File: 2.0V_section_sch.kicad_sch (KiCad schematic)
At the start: 1 part, among them U3_5 TPS259620DDAR

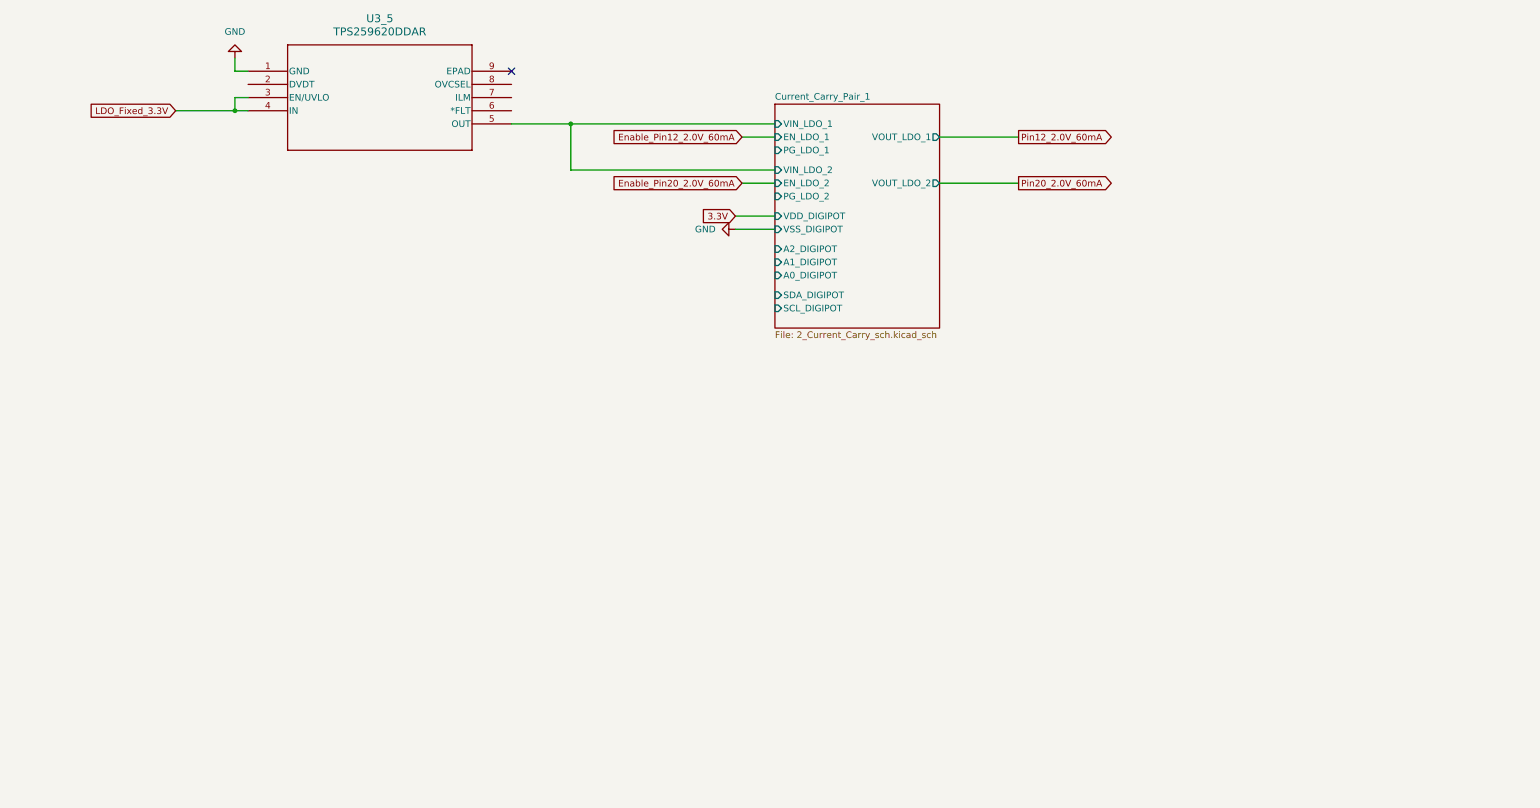
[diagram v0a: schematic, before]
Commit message: Full schematic connection without ratio consideration.
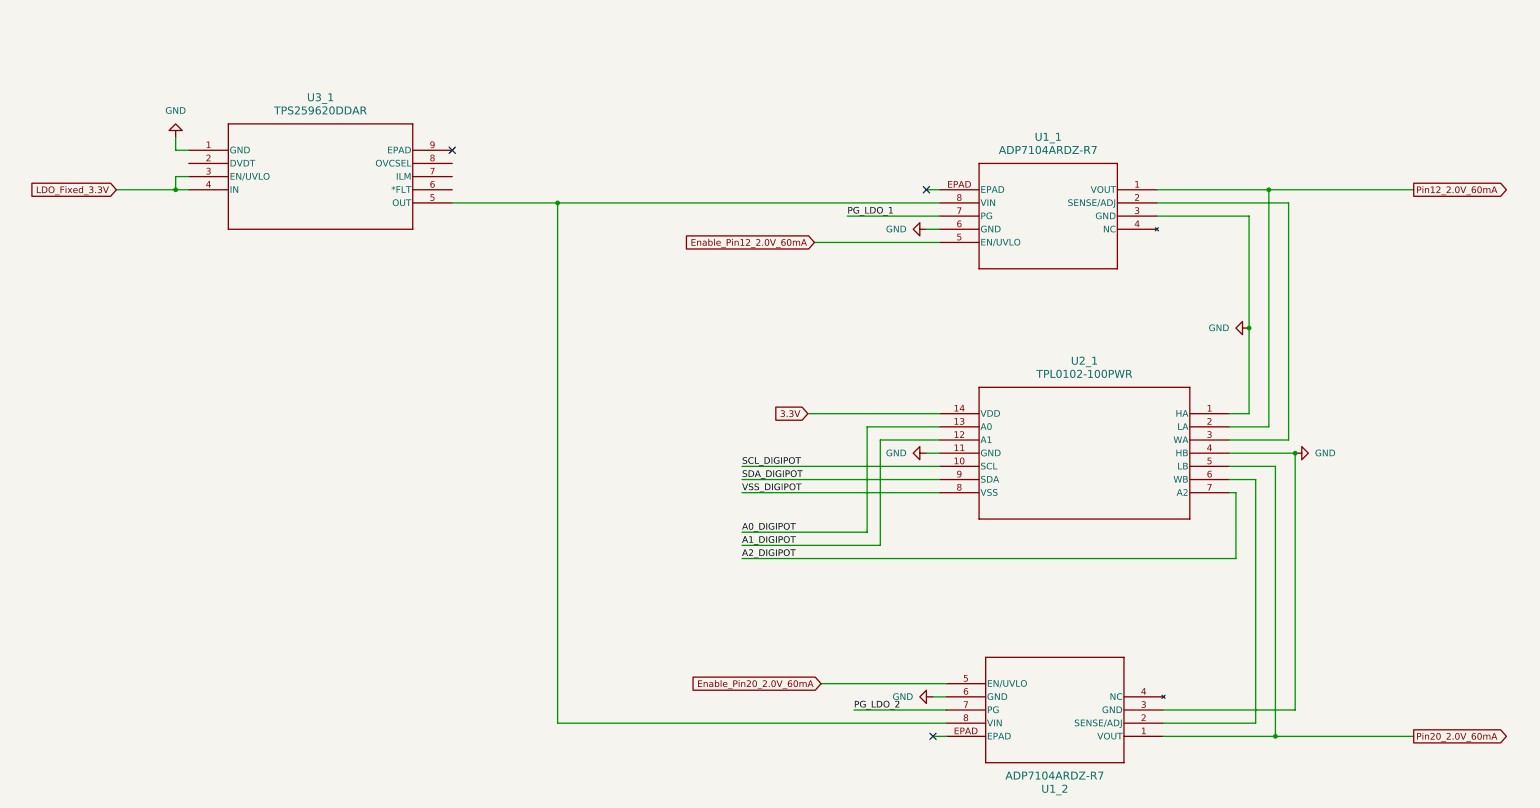
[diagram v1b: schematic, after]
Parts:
- removed U3_5: TPS259620DDAR, SOIC_20DDAR_TEX, symbol eFuse for electronic:TPS259620DDAR
- added U1_1, U1_2: ADP7104ARDZ-R7, RD_8_2_ADI, symbol Adjustable Low-Dropout Regulator:ADP7104ARDZ-R7
- added U2_1: TPL0102-100PWR, PW14, symbol Digital Potentiometer:TPL0102-100PWR
- added U3_1: TPS259620DDAR, SOIC_20DDAR_TEX, symbol eFuse for electronic:TPS259620DDAR
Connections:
- net 3.3V: now also U2_1.14 (VDD)
- net Enable_Pin12_2.0V_60mA: now also U1_1.5 (EN/UVLO)
- net Enable_Pin20_2.0V_60mA: now also U1_2.5 (EN/UVLO)
- net GND: now also U1_1.3 (GND), U1_1.6 (GND), U1_2.3 (GND), U1_2.6 (GND), U2_1.1 (HA), U2_1.11 (GND), U2_1.4 (HB), U3_1.1 (GND)
- net LDO_Fixed_3.3V: now also U3_1.3 (EN/UVLO), U3_1.4 (IN)
- net Pin12_2.0V_60mA: now also U1_1.1 (VOUT), U2_1.2 (LA)
- net Pin20_2.0V_60mA: now also U1_2.1 (VOUT), U2_1.5 (LB)
- new net: U1_1.2 (SENSE/ADJ), U2_1.3 (WA)
- new net: U1_1.8 (VIN), U1_2.8 (VIN), U3_1.5 (OUT)
- new net: U1_2.2 (SENSE/ADJ), U2_1.6 (WB)
- new net A0_DIGIPOT: U2_1.13 (A0)
- new net A1_DIGIPOT: U2_1.12 (A1)
- new net A2_DIGIPOT: U2_1.7 (A2)
- new net PG_LDO_1: U1_1.7 (PG)
- new net PG_LDO_2: U1_2.7 (PG)
- new net SCL_DIGIPOT: U2_1.10 (SCL)
- new net SDA_DIGIPOT: U2_1.9 (SDA)
- new net VSS_DIGIPOT: U2_1.8 (VSS)
- no-connect marks 1 -> 3
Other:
- removed sheet Current_Carry_Pair_1
